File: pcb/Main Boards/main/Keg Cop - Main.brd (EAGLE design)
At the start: 65 x 55.5 mm, 30 parts, among them IC1 DS18B20+, X1 RJ45-8X, X2 RJ45-8X, X3 RJ45-8X, X4 RJ45-8X

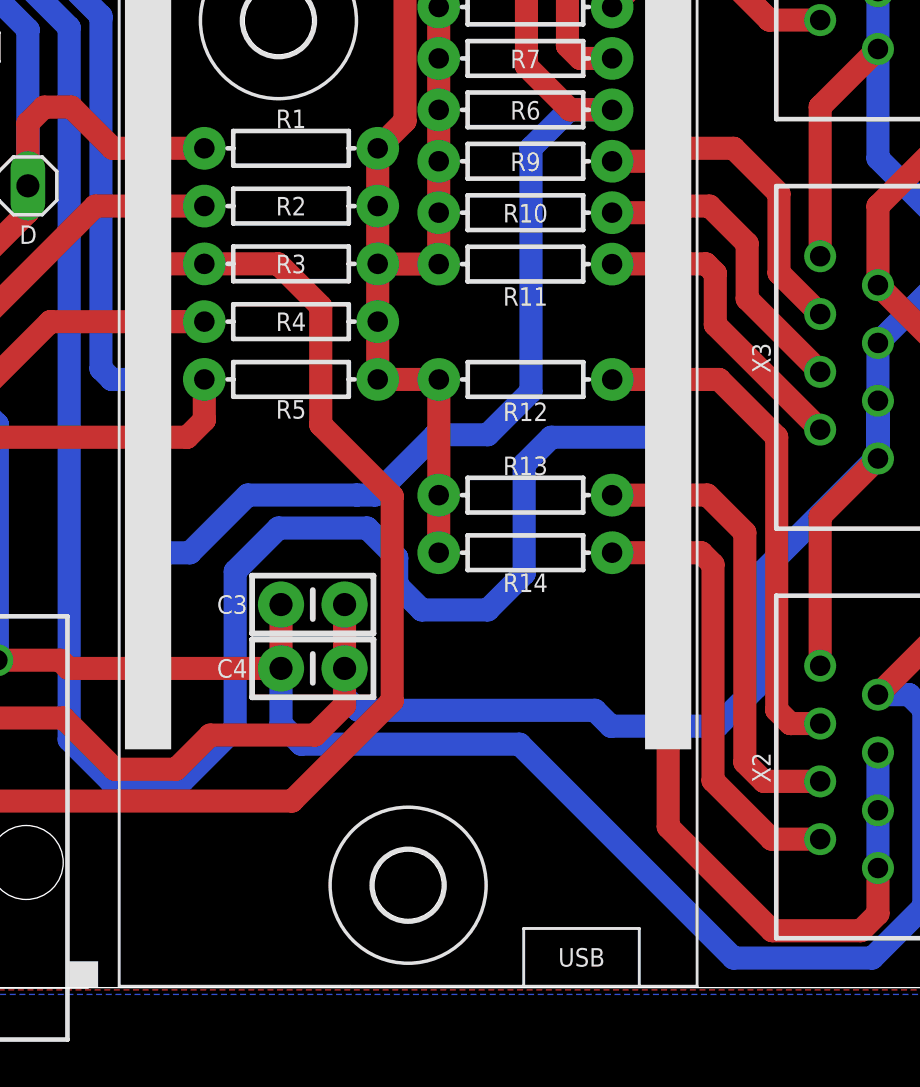
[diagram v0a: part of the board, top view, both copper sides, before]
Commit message: K0 to 4 K1 to 16 SOL to 2
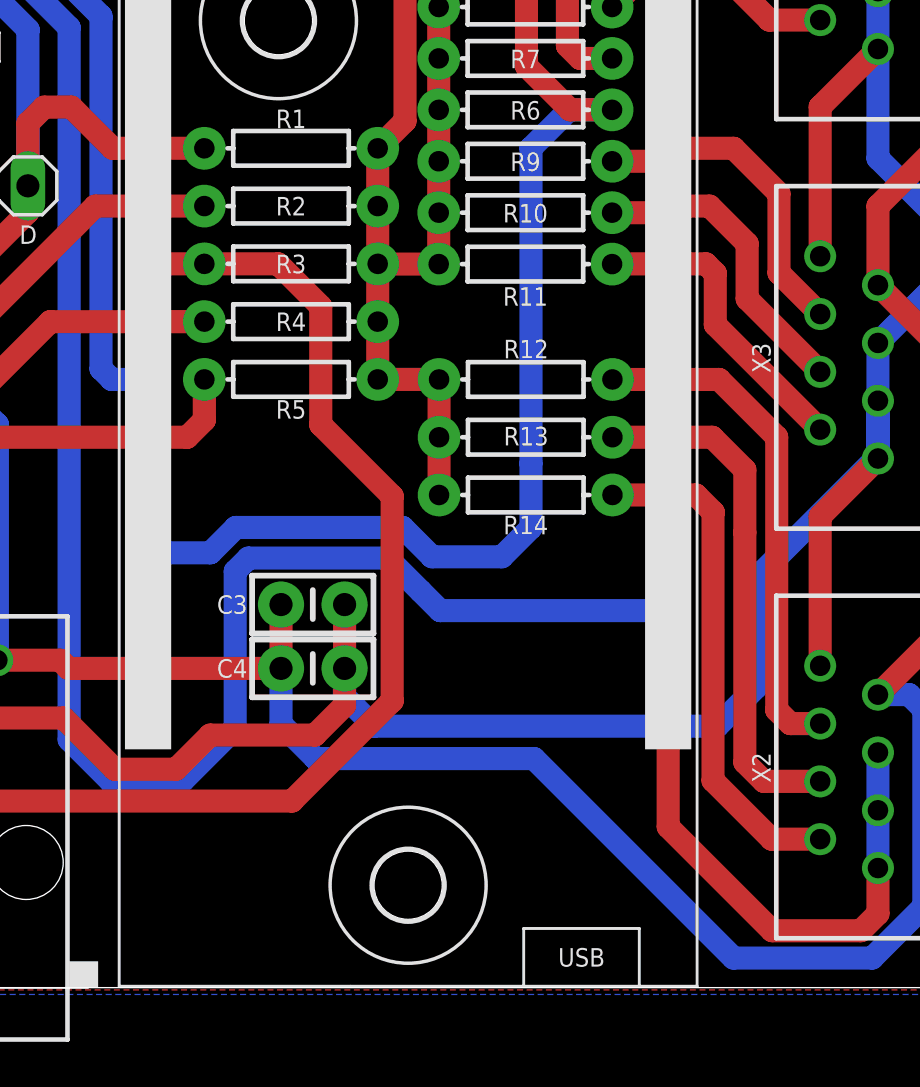
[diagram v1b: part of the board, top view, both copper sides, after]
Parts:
- moved R13 2.55 mm to (37.7, 24.2)
- moved R14 2.54 mm to (37.7, 21.7)
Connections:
- net KEG0: now also D32.IO4; no longer D32.IO0
- net KEG1: now also D32.IO16; no longer D32.IO4
- net SOL: now also D32.IO2; no longer D32.IO16
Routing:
- net SOL: track 82.7 -> 74.9 mm
- net KEG8: track 62.7 -> 67.3 mm
- net KEG1: track 20.3 -> 22.9 mm
- net 3V3: track 62.8 -> 60.3 mm
- net KEG0: track 19.9 -> 22.3 mm
